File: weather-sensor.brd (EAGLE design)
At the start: 44.7 x 147.3 mm, 31 parts, among them J1 43841-0005, J2 95501-6889, U1 SHT31, U2 MPL3115A2LGA8, U3 P82B715SOIC, U4 ADC081C021SOT-DDC, U5 MIC5219-3.3YM5-TR

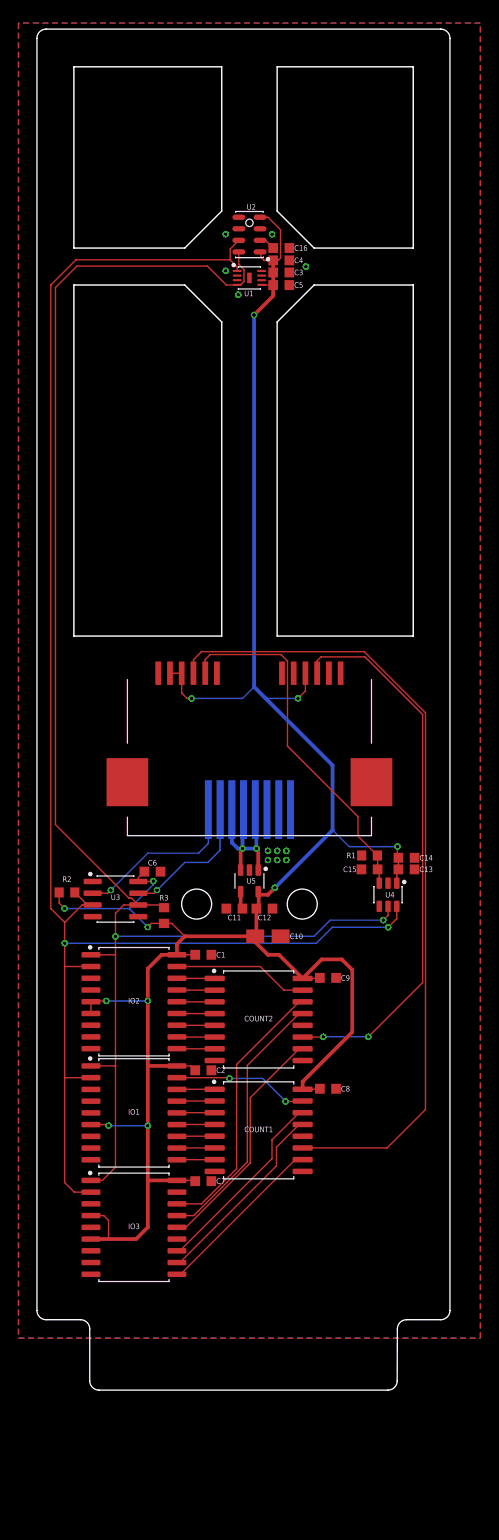
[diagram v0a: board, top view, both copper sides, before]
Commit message: Changed range extender and added debounce to switched inputs.
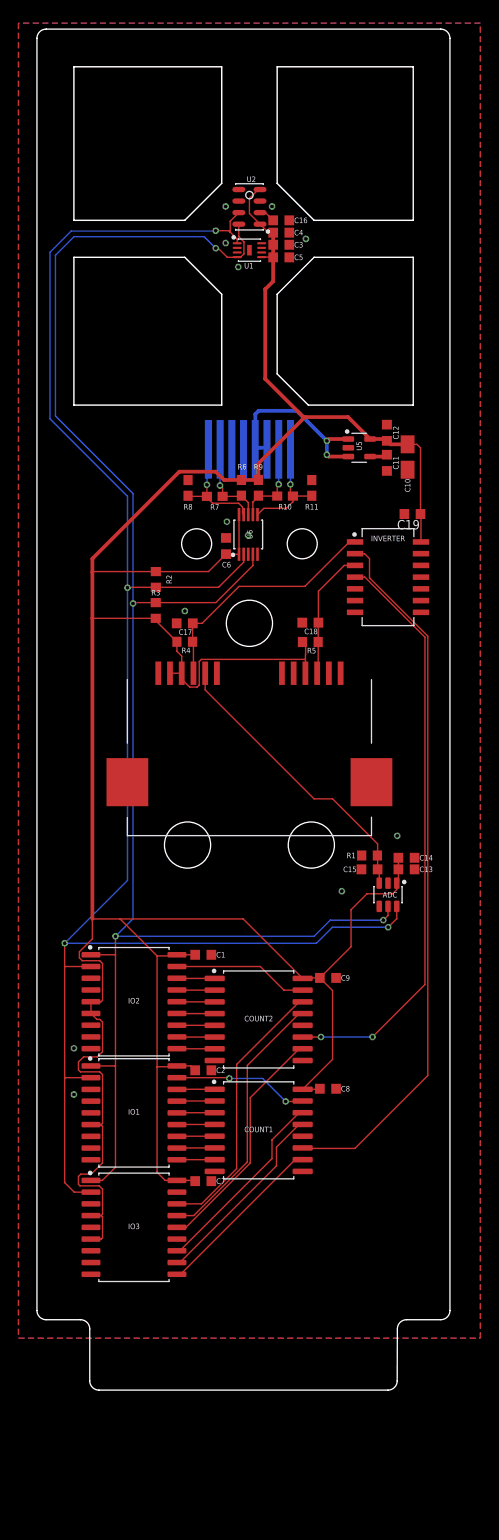
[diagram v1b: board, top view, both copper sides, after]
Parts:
- removed U3: P82B715SOIC, Conservify:SOIC127P599X175-8
- added C17, C18, C19: (no value), rcl:C0603K
- added INVERTER: 74HC14, Conservify:SOIC127P780X200-14
- added R10, R7: 100, SparkFun-Resistors:0603
- added R11, R8: 300, SparkFun-Resistors:0603
- added R4, R5: (no value), rcl:R0603
- added R6, R9: 330, SparkFun-Resistors:0603
- added U6: PCA9615, Conservify:SOP50P490X110-10
- moved C10 54.0 mm to (40.1, 101.0), turned to 90 degrees
- moved C12 53.2 mm to (37.9, 103.6), turned to 90 degrees
- moved C11 51.0 mm to (37.9, 100.4), turned to 270 degrees
- moved U5 48.4 mm to (34.9, 102.0), turned to 0 degrees
- moved J2 39.0 mm to (23.0, 91.6)
- moved C6 36.1 mm to (20.5, 91.4), turned to 90 degrees
- moved R2 35.2 mm to (12.9, 87.8), turned to 270 degrees
- moved R3 33.0 mm to (12.9, 84.4)
- moved U2 3.00 mm to (23.0, 128.1)
- moved C16 3.00 mm to (26.4, 126.6)
- moved C3 3.00 mm to (26.4, 124.0)
- moved C4 3.00 mm to (26.4, 125.3)
- moved C5 3.00 mm to (26.4, 122.6)
- moved U1 3.00 mm to (23.0, 123.4)
- renumbered U4 to ADC
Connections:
- removed net LCL: J2.7, U3.7
- removed net LDA: J2.8, U3.2
- new net !ANEM: COUNT1.11, INVERTER.2
- new net !RAIN: COUNT2.11, INVERTER.4
- new net EN: U6.3
- new net LCL-M: J2.1, R10.1, R11.2, U6.6
- new net LCL-P: J2.2, R10.2, R9.1, U6.7
- new net LDA-M: J2.8, R7.1, R8.2, U6.9
- new net LDA-P: J2.7, R6.1, R7.2, U6.8
- net 3V3: now also C19.1, INVERTER.14, R4.2, R5.2, R6.2, R9.2, U6.1, U6.10; no longer U3.8
- net ANEM: now also C17.1, INVERTER.1, R4.1; no longer COUNT1.11
- net GND: now also C17.2, C18.2, C19.2, INVERTER.7, J2.5, J2.6, R11.1, R8.1, U6.5; no longer J2.1, J2.2, J2.3, U3.4
- net RAIN: now also C18.1, INVERTER.3, R5.1; no longer COUNT2.11
- net SCL: now also U6.4; no longer U3.6
- net SDA: now also U6.2; no longer U3.3
- net UNREG: now also J2.3; no longer J2.5, J2.6
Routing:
- net 3V3: track 258.2 -> 337.2 mm, vias 12 -> 0
- net !ANEM: track 0.00 -> 77.2 mm
- net !RAIN: track 0.00 -> 63.4 mm, vias 0 -> 2
- net ANEM: track 87.6 -> 26.8 mm
- net RAIN: track 60.0 -> 14.1 mm, vias 2 -> 0
- net LDA: track 18.4 -> 0.00 mm, vias 1 -> 0
- net SDA: track 175.6 -> 193.5 mm, vias 2 -> 4
- net LCL: track 15.2 -> 0.00 mm, vias 1 -> 0
- net SCL: track 169.7 -> 184.6 mm, vias 2 -> 4
- net LDA-M: track 0.00 -> 12.5 mm, vias 0 -> 1
- net LCL-M: track 0.00 -> 12.3 mm, vias 0 -> 1
- net LDA-P: track 0.00 -> 9.64 mm, vias 0 -> 1
- net LCL-P: track 0.00 -> 9.46 mm, vias 0 -> 1
- net VANE: track 39.1 -> 31.7 mm
- net UNREG: track 19.8 -> 20.7 mm
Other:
- outline, holes or cut-outs redrawn

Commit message: Changed power architecture for module/sesnor power synchronization. TA4.
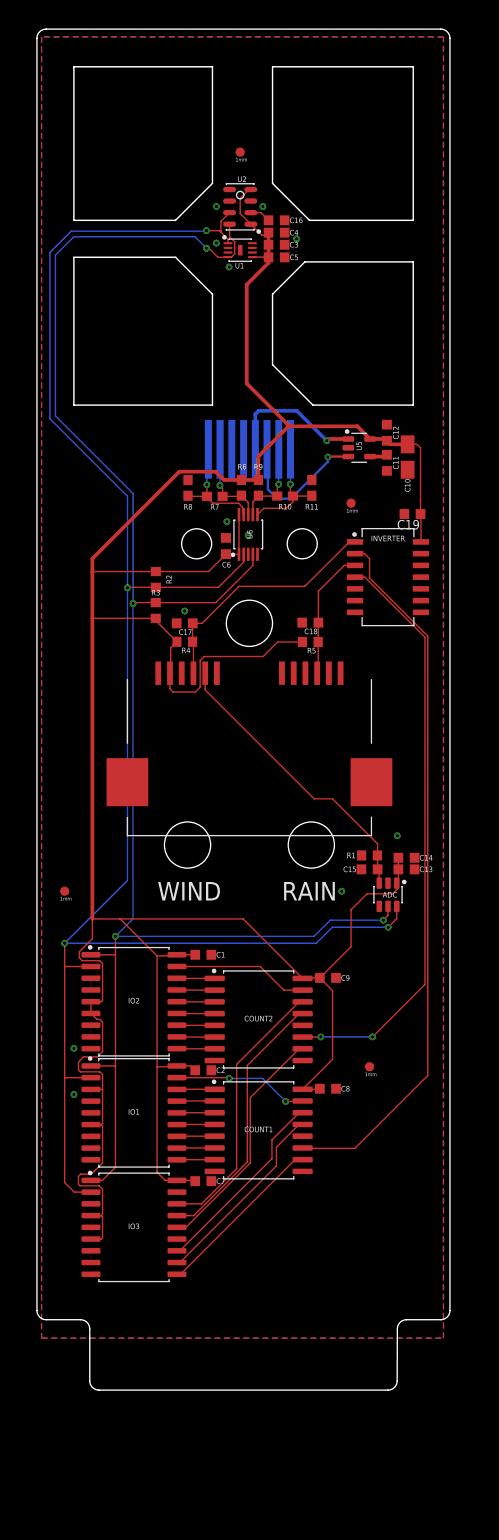
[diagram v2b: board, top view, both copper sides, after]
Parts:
- added FID1, FID2, FID3, FID4: FIDUCIAL1X2.5, microbuilder:FIDUCIAL-1X2.5
- C13: value (none) -> .1u
- C14: value (none) -> 4.7u
- C15: value (none) -> 470p
- C17, C18: value (none) -> 1uf
- R1, R4, R5: value (none) -> 10k
- moved U1 1.00 mm to (22.0, 123.4)
- moved U2 1.00 mm to (22.0, 128.1)
- moved C16 0.50 mm to (25.9, 126.6)
- moved C3 0.50 mm to (25.9, 124.0)
- moved C4 0.50 mm to (25.9, 125.3)
- moved C5 0.50 mm to (25.9, 122.6)
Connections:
- net N$11 renamed 2OE
- net N$21 renamed 2RCLK
- net N$22 renamed 2CCLR
- new net ENABLE: J2.3, U5.3
- net 3V3: now also IO1.3; no longer J1.A3, J1.B3
- net GND: now also J1.A3, J1.B3; no longer IO1.3
- net UNREG: no longer J2.3, U5.3
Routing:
- net ENABLE: track 0.00 -> 15.7 mm, vias 0 -> 1
- net UNREG: track 20.7 -> 15.5 mm, vias 2 -> 1
- net 3V3: track 337.2 -> 339.5 mm
- net SDA: track 193.5 -> 192.5 mm
- net SCL: track 184.6 -> 183.6 mm
- net CAP: track 1.76 -> 2.26 mm
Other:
- outline, holes or cut-outs redrawn
- board text added: "RAIN"
- board text added: "WIND"

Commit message: New Panel
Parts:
- C1, C19, C2, C3, C6, C7, C8, C9: value (none) -> .1uf
- C11: value (none) -> 470pf
- C13: value .1u -> .1uf
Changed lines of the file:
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@@
 <attribute name="NAME" x="10.5" y="17.42495" size="0.6" layer="25" ratio="20" align="bottom-center"/>
 </element>
-<element name="C1" library="rcl" library_urn="urn:adsk.eagle:library:334" package="C0603K" package3d_urn="urn:adsk.eagle:package:23680/2" value="" x="18" y="47.12" smashed="yes">
+<element name="C1" library="rcl" library_urn="urn:adsk.eagle:library:334" package="C0603K" package3d_urn="urn:adsk.eagle:package:23680/2" value=".1uf" x="18" y="47.12" smashed="yes">
 <attribute name="NAME" x="19.4" y="47.12" size="0.6" layer="25" ratio="20" align="center-left"/>
 <attribute name="SPICEPREFIX" value="C" x="18" y="47.12" size="1.778" layer="27" display="off"/>
 <attribute name="VALUE" x="17.2" y="45.47" size="1.016" layer="27"/>
 </element>
-<element name="C2" library="rcl" library_urn="urn:adsk.eagle:library:334" package="C0603K" package3d_urn="urn:adsk.eagle:package:23680/2" value="" x="18" y="34.62" smashed="yes">
+<element name="C2" library="rcl" library_urn="urn:adsk.eagle:library:334" package="C0603K" package3d_urn="urn:adsk.eagle:package:23680/2" value=".1uf" x="18" y="34.62" smashed="yes">
 <attribute name="NAME" x="19.4" y="34.62" size="0.6" layer="25" ratio="20" align="center-left"/>
 <attribute name="SPICEPREFIX" value="C" x="18" y="34.62" size="1.778" layer="27" display="off"/>
 <attribute name="VALUE" x="17.2" y="32.97" size="1.016" layer="27"/>
 </element>
-<element name="C3" library="rcl" library_urn="urn:adsk.eagle:library:334" package="C0603K" package3d_urn="urn:adsk.eagle:package:23680/2" value="" x="25.9405" y="123.978" smashed="yes">
+<element name="C3" library="rcl" library_urn="urn:adsk.eagle:library:334" package="C0603K" package3d_urn="urn:adsk.eagle:package:23680/2" value=".1uf" x="25.9405" y="123.978" smashed="yes">
 <attribute name="NAME" x="27.3405" y="123.978" size="0.6" layer="25" ratio="20" align="center-left"/>
 <attribute name="SPICEPREFIX" value="C" x="25.9405" y="123.978" size="1.778" layer="27" display="off"/>
@@
 <attribute name="SPICEPREFIX" value="C" x="25.9405" y="122.614278125" size="1.778" layer="27" display="off"/>
 </element>
-<element name="C6" library="rcl" library_urn="urn:adsk.eagle:library:334" package="C0603K" package3d_urn="urn:adsk.eagle:package:23680/2" value="" x="20.461" y="91.367" smashed="yes" rot="R90">
+<element name="C6" library="rcl" library_urn="urn:adsk.eagle:library:334" package="C0603K" package3d_urn="urn:adsk.eagle:package:23680/2" value=".1uf" x="20.461" y="91.367" smashed="yes" rot="R90">
 <attribute name="NAME" x="20.52" y="89.644" size="0.6" layer="25" ratio="20" rot="R180" align="bottom-center"/>
 <attribute name="SPICEPREFIX" value="C" x="20.461" y="91.367" size="1.778" layer="27" rot="R90" display="off"/>
 <attribute name="VALUE" x="22.111" y="90.567" size="1.016" layer="27" rot="R90"/>
 </element>
-<element name="C7" library="rcl" library_urn="urn:adsk.eagle:library:334" package="C0603K" package3d_urn="urn:adsk.eagle:package:23680/2" value="" x="18" y="22.62" smashed="yes" rot="R180">
+<element name="C7" library="rcl" library_urn="urn:adsk.eagle:library:334" package="C0603K" package3d_urn="urn:adsk.eagle:package:23680/2" value=".1uf" x="18" y="22.62" smashed="yes" rot="R180">
 <attribute name="NAME" x="19.4" y="22.62" size="0.6" layer="25" ratio="20" align="center-left"/>
 <attribute name="SPICEPREFIX" value="C" x="18" y="22.62" size="1.778" layer="27" rot="R180" display="off"/>
 <attribute name="VALUE" x="18.8" y="24.27" size="1.016" layer="27" rot="R180"/>
 </element>
-<element name="C8" library="rcl" library_urn="urn:adsk.eagle:library:334" package="C0603K" package3d_urn="urn:adsk.eagle:package:23680/2" value="" x="31.5" y="32.62" smashed="yes">
+<element name="C8" library="rcl" library_urn="urn:adsk.eagle:library:334" package="C0603K" package3d_urn="urn:adsk.eagle:package:23680/2" value=".1uf" x="31.5" y="32.62" smashed="yes">
 <attribute name="NAME" x="32.9" y="32.62" size="0.6" layer="25" ratio="20" align="center-left"/>
 <attribute name="SPICEPREFIX" value="C" x="31.5" y="32.62" size="1.778" layer="27" display="off"/>
 <attribute name="VALUE" x="30.7" y="30.97" size="1.016" layer="27"/>
 </element>
-<element name="C9" library="rcl" library_urn="urn:adsk.eagle:library:334" package="C0603K" package3d_urn="urn:adsk.eagle:package:23680/2" value="" x="31.5" y="44.62" smashed="yes">
+<element name="C9" library="rcl" library_urn="urn:adsk.eagle:library:334" package="C0603K" package3d_urn="urn:adsk.eagle:package:23680/2" value=".1uf" x="31.5" y="44.62" smashed="yes">
 <attribute name="NAME" x="32.9" y="44.62" size="0.6" layer="25" ratio="20" align="center-left"/>
 <attribute name="SPICEPREFIX" value="C" x="31.5" y="44.62" size="1.778" layer="27" display="off"/>
@@
 <attribute name="SPICEPREFIX" value="C" x="31.62" y="87.5" size="1.778" layer="27" rot="R90" display="off"/>
 </element>
-<element name="C11" library="rcl" library_urn="urn:adsk.eagle:library:334" package="C0603K" package3d_urn="urn:adsk.eagle:package:23680/2" value="" x="37.88" y="100.373" smashed="yes" rot="R270">
+<element name="C11" library="rcl" library_urn="urn:adsk.eagle:library:334" package="C0603K" package3d_urn="urn:adsk.eagle:package:23680/2" value="470pf" x="37.88" y="100.373" smashed="yes" rot="R270">
 <attribute name="NAME" x="38.547" y="100.373" size="0.6" layer="25" ratio="20" rot="R90" align="top-center"/>
 <attribute name="SPICEPREFIX" value="C" x="46.38" y="114.373" size="1.778" layer="27" rot="R270" display="off"/>
@@
 <attribute name="NAME" x="38.20995" y="53.32" size="0.6" layer="25" ratio="20" align="bottom-center"/>
 </element>
-<element name="C13" library="rcl" library_urn="urn:adsk.eagle:library:334" package="C0603K" package3d_urn="urn:adsk.eagle:package:23680/2" value=".1u" x="40" y="56.37" smashed="yes">
+<element name="C13" library="rcl" library_urn="urn:adsk.eagle:library:334" package="C0603K" package3d_urn="urn:adsk.eagle:package:23680/2" value=".1uf" x="40" y="56.37" smashed="yes">
 <attribute name="NAME" x="41.4" y="56.37" size="0.6" layer="25" ratio="20" align="center-left"/>
 <attribute name="SPICEPREFIX" value="C" x="40" y="56.37" size="1.778" layer="27" display="off"/>
@@
 <attribute name="PROD_ID" value="RES-07828" x="22.751" y="113.659" size="1.778" layer="27" rot="R270" display="off"/>
 </element>
-<element name="C19" library="rcl" library_urn="urn:adsk.eagle:library:334" package="C0603K" package3d_urn="urn:adsk.eagle:package:23680/2" value="" x="40.646" y="94.832" smashed="yes" rot="R180">
+<element name="C19" library="rcl" library_urn="urn:adsk.eagle:library:334" package="C0603K" package3d_urn="urn:adsk.eagle:package:23680/2" value=".1uf" x="40.646" y="94.832" smashed="yes" rot="R180">
 <attribute name="NAME" x="41.446" y="94.182" size="1.016" layer="25" rot="R180"/>
 <attribute name="SPICEPREFIX" value="C" x="40.646" y="94.832" size="1.778" layer="27" rot="R180" display="off"/>

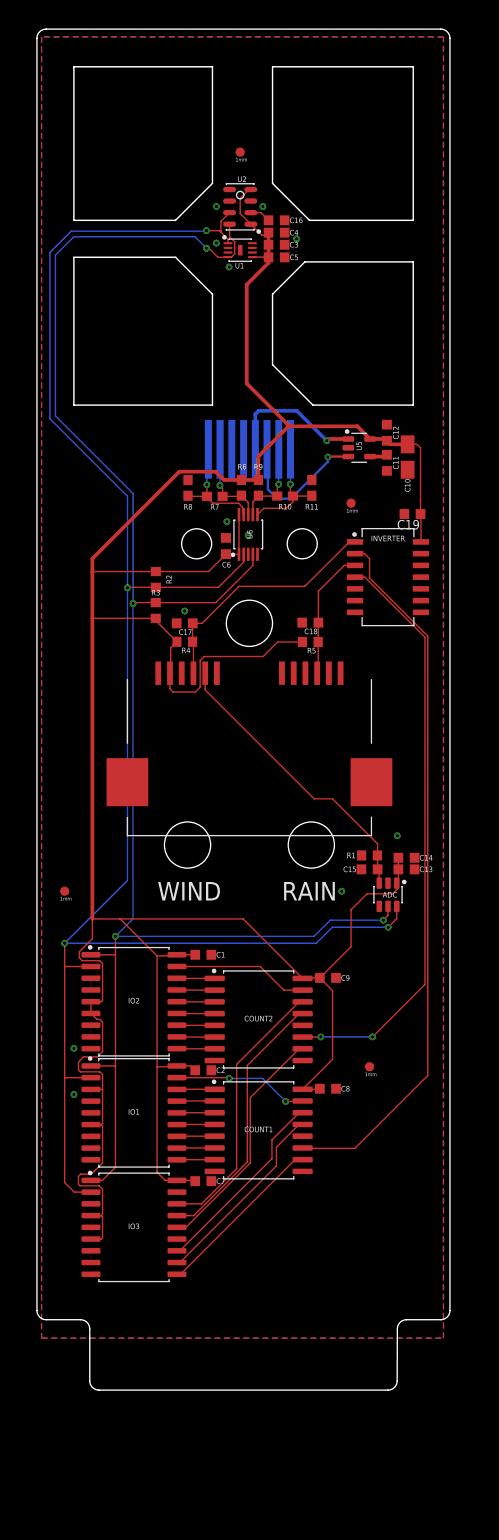
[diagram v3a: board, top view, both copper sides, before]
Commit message: Replaced sensors with BME280, Reworked outline for compatibility with new arm.
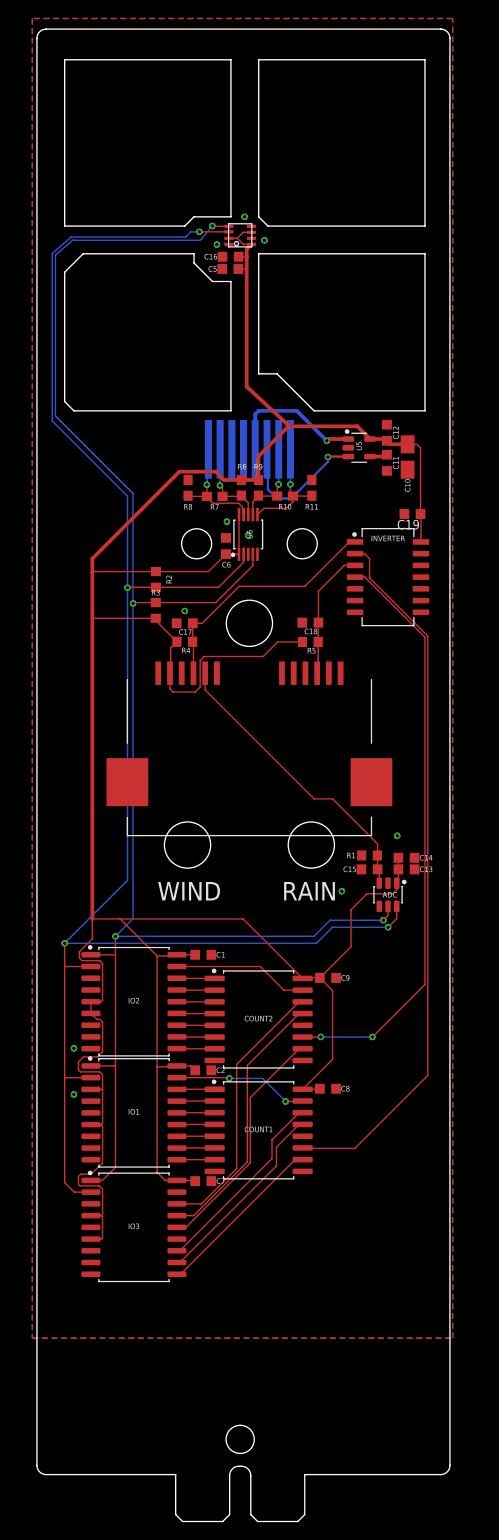
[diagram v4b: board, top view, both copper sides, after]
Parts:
- removed C3: .1uf, rcl:C0603K
- removed C4: 10uf, rcl:C0603K
- removed FID1, FID2, FID3, FID4: FIDUCIAL1X2.5, microbuilder:FIDUCIAL-1X2.5
- removed U2: MPL3115A2LGA8, Conservify:SON125P300X500X110-8
- U1: value SHT31 -> BME280; device Conservify:SON50P240X240X80-9T80 -> Conservify:BM280
- moved C16 6.35 mm to (21.0, 122.7), turned to 180 degrees
- moved C5 5.17 mm to (20.9, 121.4), turned to 180 degrees
- moved U1 1.61 mm to (22.0, 125.0), turned to 180 degrees
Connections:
- removed net CAP: C16.1, U2.2
- net 3V3: now also C16.1, U1.2, U1.6, U1.8; no longer C3.1, C4.1, U1.5, U2.1, U2.4
- net GND: now also U1.1, U1.5; no longer C3.2, C4.2, U1.2, U1.8, U2.3
- net SCL: no longer U2.8
- net SDA: now also U1.3; no longer U1.1, U2.7
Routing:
- net 3V3: track 339.5 -> 334.8 mm
- net SCL: track 183.6 -> 179.0 mm
- net SDA: track 192.5 -> 188.7 mm
- net CAP: track 2.26 -> 0.00 mm
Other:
- board size 44.7 x 147.3 mm -> 44.7 x 161.5 mm
